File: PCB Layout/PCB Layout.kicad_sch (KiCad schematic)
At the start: 15 parts, among them J1 Conn_01x15, J2 Conn_01x15, J3 Screw_Terminal_01x04, J4 Conn_01x02

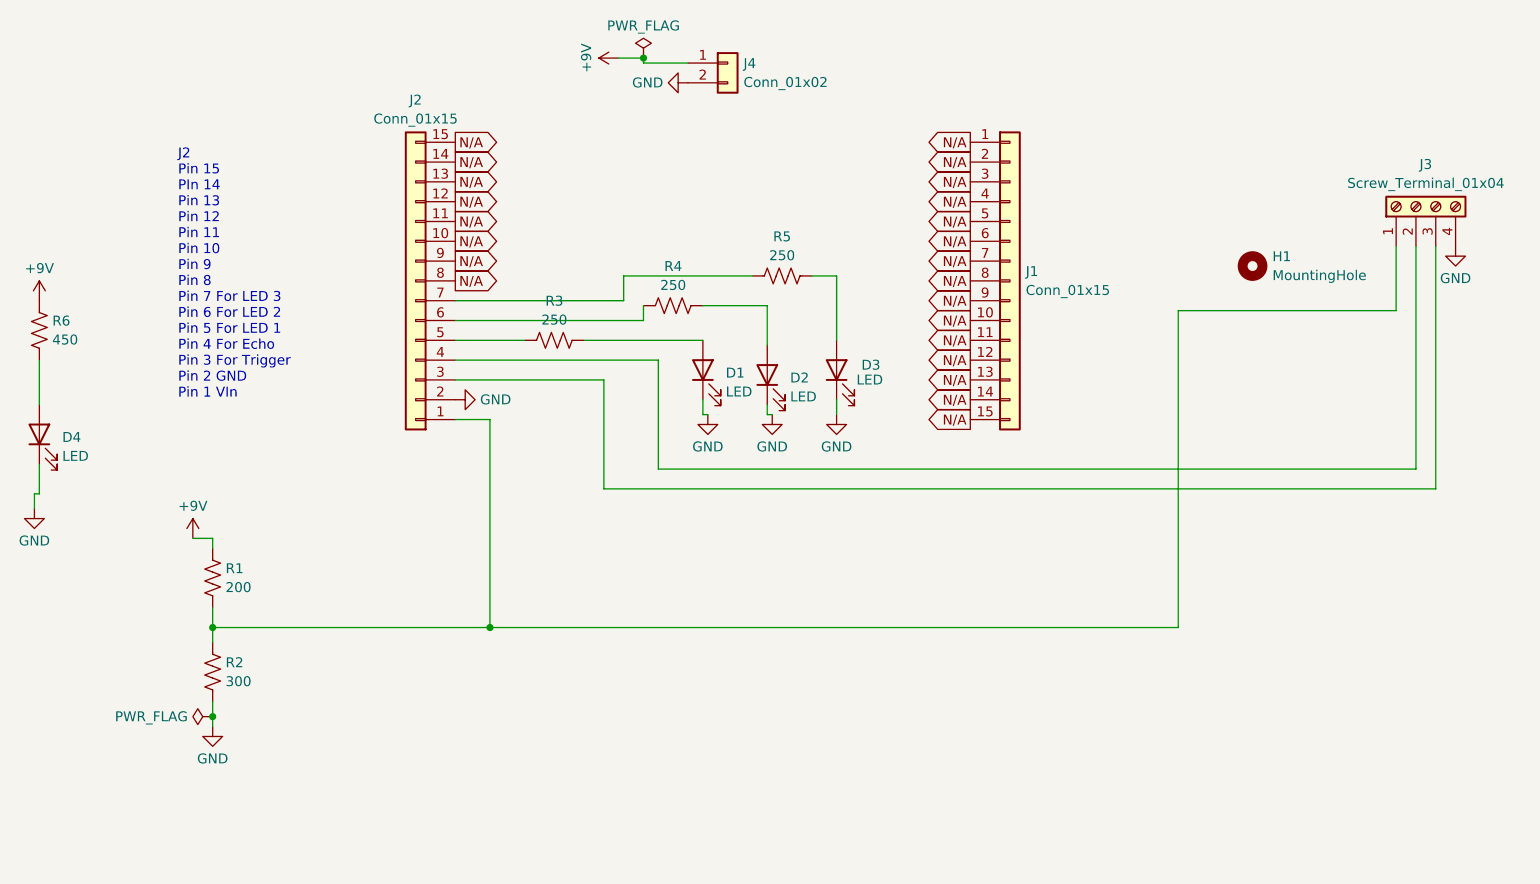
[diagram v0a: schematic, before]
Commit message: This increased the esp32 footprint to be spaced by 26.25 mm
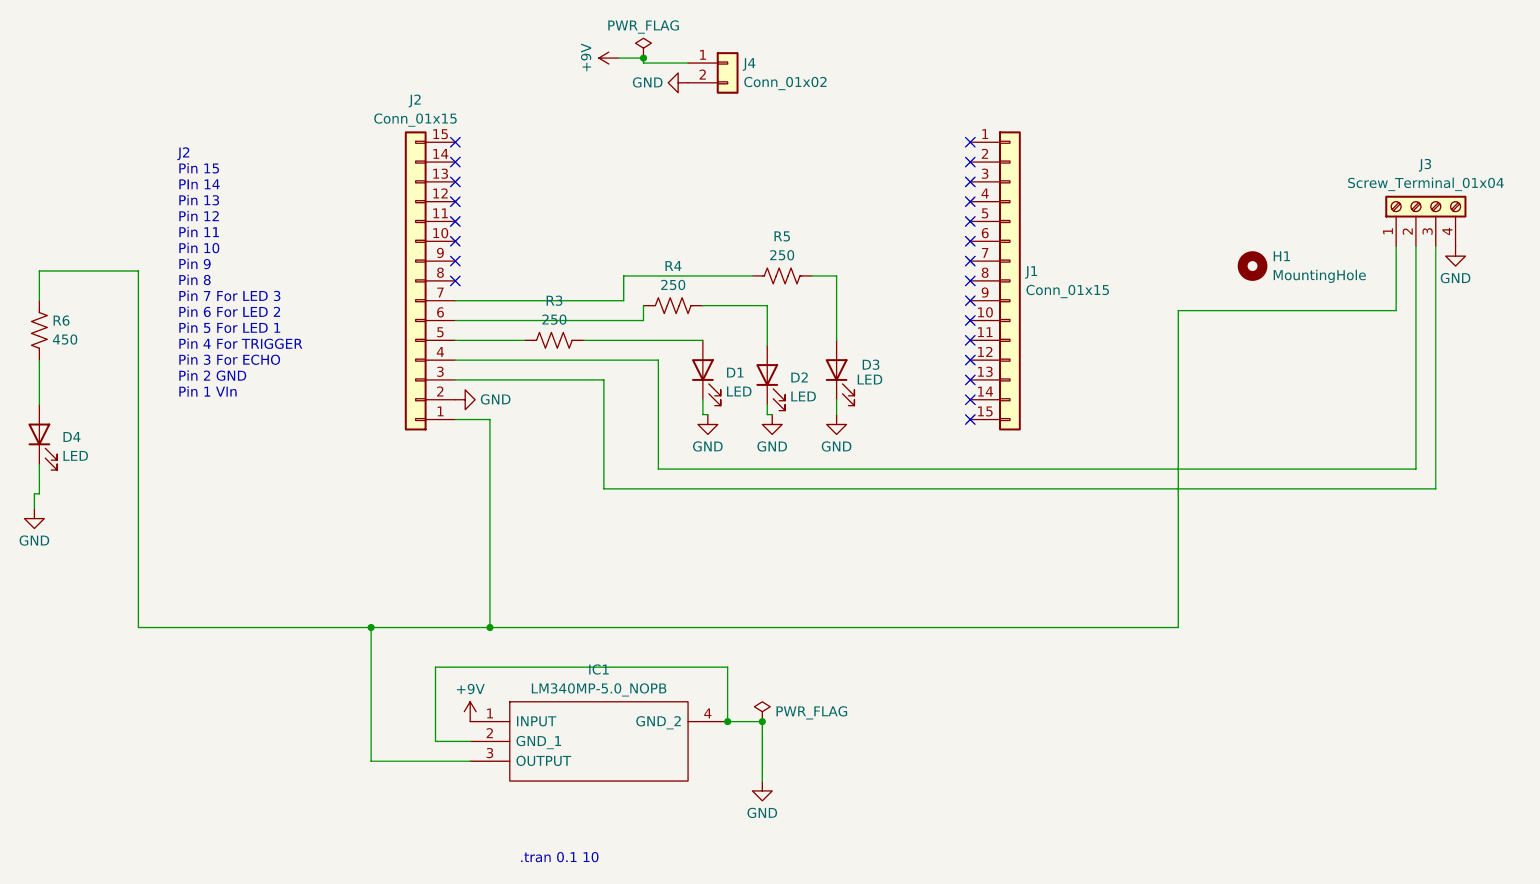
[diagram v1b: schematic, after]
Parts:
- removed R1: 200, Resistor_THT:R_Axial_DIN0207_L6.3mm_D2.5mm_P7.62mm_Horizontal, symbol Device:R_US
- removed R2: 300, Resistor_THT:R_Axial_DIN0207_L6.3mm_D2.5mm_P7.62mm_Horizontal, symbol Device:R_US
- added IC1: LM340MP-5.0_NOPB, SamacSys:SOT230P700X180-4N, symbol Library SamacSys:LM340MP-5.0_NOPB
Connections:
- net +9V: now also IC1.1 (INPUT); no longer R6.1
- net GND: now also IC1.2 (GND_1), IC1.4 (GND_2)
- net at J2.1 (Pin_1), J3.1 (Pin_1): now also R6.1, IC1.3 (OUTPUT)
- removed net N/A: J1.1 (Pin_1), J1.10 (Pin_10), J1.11 (Pin_11), J1.12 (Pin_12), J1.13 (Pin_13), J1.14 (Pin_14), J1.15 (Pin_15), J1.2 (Pin_2), J1.3 (Pin_3), J1.4 (Pin_4), J1.5 (Pin_5), J1.6 (Pin_6), J1.7 (Pin_7), J1.8 (Pin_8), J1.9 (Pin_9), J2.10 (Pin_10), J2.11 (Pin_11), J2.12 (Pin_12), J2.13 (Pin_13), J2.14 (Pin_14), J2.15 (Pin_15), J2.8 (Pin_8), J2.9 (Pin_9)
- no-connect marks 0 -> 23
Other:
- note added: ".tran 0.1 10"
- note added: "J2 Pin 15 PIn 14 Pin 13 Pin 12 Pin 11 Pin 10 Pin 9 Pin 8 Pin 7 For LED 3 Pin 6 For LED 2 Pin 5 For LED 1 Pin 4 For TRIGGER Pin 3 For ECHO Pin 2 GND Pin 1 VIn"
- note removed: "J2 Pin 15 PIn 14 Pin 13 Pin 12 Pin 11 Pin 10 Pin 9 Pin 8 Pin 7 For LED 3 Pin 6 For LED 2 Pin 5 For LED 1 Pin 4 For Echo Pin 3 For Trigger Pin 2 GND Pin 1 VIn"
